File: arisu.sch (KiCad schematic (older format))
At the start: 28 parts, among them J1 USB_B_Micro, J10 PF6, J11 PF7, J2 MISO, J3 VCC, J4 SCK, J5 MOSI, J6 RES, J7 GND, J8 PF4, J9 PF5, U1 USBLC6-2SC6, U2 ATmega32U4-AU, Y1 Crystal_GND24

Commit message: Assign PCB footprints to schematic symbols
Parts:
- C1, C2, C3, C4, C5, C6, C7, C8, C9: footprint (none) -> Capacitors_SMD:C_0805_HandSoldering
- J1: footprint (none) -> Connectors_USB:USB_Micro-B_Molex-105017-0001
- J10, J11, J2, J3, J4, J5, J6, J7, J8, J9: footprint (none) -> Pin_Headers:Pin_Header_Straight_1x01_Pitch2.54mm
- R1, R2, R3, R4: footprint (none) -> Resistors_SMD:R_0805_HandSoldering
- SWR1: footprint (none) -> Buttons_Switches_SMD:SW_SPST_TL3342
- Y1: footprint (none) -> Crystals:Crystal_SMD_SeikoEpson_FA238-4pin_3.2x2.5mm_HandSoldering
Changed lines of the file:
@@
 F 0 "J1" H 1055 5267 50  0000 C CNN
 F 1 "USB_B_Micro" H 1055 5176 50  0000 C CNN
-F 2 "" H 1150 4750 50  0001 C CNN
+F 2 "Connectors_USB:USB_Micro-B_Molex-105017-0001" H 1150 4750 50  0001 C CNN
 F 3 "~" H 1150 4750 50  0001 C CNN
 	1    1000 4800
@@
 F 0 "R1" V 2550 4800 50  0000 C CNN
 F 1 "22" V 2650 4800 50  0000 C CNN
-F 2 "" V 2580 4800 50  0001 C CNN
+F 2 "Resistors_SMD:R_0805_HandSoldering" V 2580 4800 50  0001 C CNN
 F 3 "~" H 2650 4800 50  0001 C CNN
 	1    2650 4800
@@
 F 0 "R2" V 2750 4900 50  0000 C CNN
 F 1 "22" V 2650 4900 50  0000 C CNN
-F 2 "" V 2580 4900 50  0001 C CNN
+F 2 "Resistors_SMD:R_0805_HandSoldering" V 2580 4900 50  0001 C CNN
 F 3 "~" H 2650 4900 50  0001 C CNN
 	1    2650 4900
@@
 F 0 "C4" H 3765 4246 50  0000 L CNN
 F 1 "1uF (±10%)" H 3765 4155 50  0000 L CNN
-F 2 "" H 3688 4050 50  0001 C CNN
+F 2 "Capacitors_SMD:C_0805_HandSoldering" H 3688 4050 50  0001 C CNN
 F 3 "~" H 3650 4200 50  0001 C CNN
 	1    3650 4200
@@
 F 0 "Y1" H 1850 4000 50  0000 L CNN
 F 1 "Crystal_GND24" H 1650 3900 50  0000 L CNN
-F 2 "" H 1900 3650 50  0001 C CNN
+F 2 "Crystals:Crystal_SMD_SeikoEpson_FA238-4pin_3.2x2.5mm_HandSoldering" H 1900 3650 50  0001 C CNN
 F 3 "~" H 1900 3650 50  0001 C CNN
 	1    1900 3650
@@
 F 0 "C1" H 1436 3754 50  0000 R CNN
 F 1 "22pF" H 1436 3845 50  0000 R CNN
-F 2 "" H 1588 3650 50  0001 C CNN
+F 2 "Capacitors_SMD:C_0805_HandSoldering" H 1588 3650 50  0001 C CNN
 F 3 "~" H 1550 3800 50  0001 C CNN
 	1    1550 3800
@@
 F 0 "C2" H 2365 3846 50  0000 L CNN
 F 1 "22pF" H 2365 3755 50  0000 L CNN
-F 2 "" H 2288 3650 50  0001 C CNN
+F 2 "Capacitors_SMD:C_0805_HandSoldering" H 2288 3650 50  0001 C CNN
 F 3 "~" H 2250 3800 50  0001 C CNN
 	1    2250 3800
@@
 F 0 "C3" H 3365 4246 50  0000 L CNN
 F 1 "10uF" H 3365 4155 50  0000 L CNN
-F 2 "" H 3288 4050 50  0001 C CNN
+F 2 "Capacitors_SMD:C_0805_HandSoldering" H 3288 4050 50  0001 C CNN
 F 3 "~" H 3250 4200 50  0001 C CNN
 	1    3250 4200
@@
 F 0 "SWR1" H 3400 3035 50  0000 C CNN
 F 1 "SW_Push" H 3400 2944 50  0000 C CNN
-F 2 "" H 3400 2950 50  0001 C CNN
+F 2 "Buttons_Switches_SMD:SW_SPST_TL3342" H 3400 2950 50  0001 C CNN
 F 3 "" H 3400 2950 50  0001 C CNN
 	1    3400 2750
@@
 F 0 "R3" H 3870 2596 50  0000 L CNN
 F 1 "10K" V 3800 2500 50  0000 L CNN
-F 2 "" V 3730 2550 50  0001 C CNN
+F 2 "Resistors_SMD:R_0805_HandSoldering" V 3730 2550 50  0001 C CNN
 F 3 "~" H 3800 2550 50  0001 C CNN
 	1    3800 2550
@@
 F 0 "C5" H 5365 1196 50  0000 L CNN
 F 1 "1uF" H 5365 1105 50  0000 L CNN
-F 2 "" H 5288 1000 50  0001 C CNN
+F 2 "Capacitors_SMD:C_0805_HandSoldering" H 5288 1000 50  0001 C CNN
 F 3 "~" H 5250 1150 50  0001 C CNN
 	1    5250 1150
@@
 F 0 "C6" H 5365 1746 50  0000 L CNN
 F 1 "0.1uF" H 5365 1655 50  0000 L CNN
-F 2 "" H 5288 1550 50  0001 C CNN
+F 2 "Capacitors_SMD:C_0805_HandSoldering" H 5288 1550 50  0001 C CNN
 F 3 "~" H 5250 1700 50  0001 C CNN
 	1    5250 1700
@@
 F 0 "C8" H 5815 1746 50  0000 L CNN
 F 1 "0.1uF" H 5815 1655 50  0000 L CNN
-F 2 "" H 5738 1550 50  0001 C CNN
+F 2 "Capacitors_SMD:C_0805_HandSoldering" H 5738 1550 50  0001 C CNN
 F 3 "~" H 5700 1700 50  0001 C CNN
 	1    5700 1700
@@
 F 0 "C7" H 5365 2296 50  0000 L CNN
 F 1 "0.1uF" H 5365 2205 50  0000 L CNN
-F 2 "" H 5288 2100 50  0001 C CNN
+F 2 "Capacitors_SMD:C_0805_HandSoldering" H 5288 2100 50  0001 C CNN
 F 3 "~" H 5250 2250 50  0001 C CNN
 	1    5250 2250
@@
 F 0 "C9" H 5815 2296 50  0000 L CNN
 F 1 "0.1uF" H 5815 2205 50  0000 L CNN
-F 2 "" H 5738 2100 50  0001 C CNN
+F 2 "Capacitors_SMD:C_0805_HandSoldering" H 5738 2100 50  0001 C CNN
 F 3 "~" H 5700 2250 50  0001 C CNN
 	1    5700 2250
@@
 F 0 "R4" H 5770 5946 50  0000 L CNN
 F 1 "10K" V 5700 5850 50  0000 L CNN
-F 2 "" V 5630 5900 50  0001 C CNN
+F 2 "Resistors_SMD:R_0805_HandSoldering" V 5630 5900 50  0001 C CNN
 F 3 "~" H 5700 5900 50  0001 C CNN
 	1    5700 5900
@@
 F 0 "J8" H 6179 6642 50  0000 L CNN
 F 1 "PF4" H 6179 6551 50  0000 L CNN
-F 2 "" H 6100 6600 50  0001 C CNN
+F 2 "Pin_Headers:Pin_Header_Straight_1x01_Pitch2.54mm" H 6100 6600 50  0001 C CNN
 F 3 "~" H 6100 6600 50  0001 C CNN
 	1    6100 6600
@@
 F 0 "J9" H 6179 6842 50  0000 L CNN
 F 1 "PF5" H 6179 6751 50  0000 L CNN
-F 2 "" H 6100 6800 50  0001 C CNN
+F 2 "Pin_Headers:Pin_Header_Straight_1x01_Pitch2.54mm" H 6100 6800 50  0001 C CNN
 F 3 "~" H 6100 6800 50  0001 C CNN
 	1    6100 6800
@@
 F 0 "J10" H 6179 7042 50  0000 L CNN
 F 1 "PF6" H 6179 6951 50  0000 L CNN
-F 2 "" H 6100 7000 50  0001 C CNN
+F 2 "Pin_Headers:Pin_Header_Straight_1x01_Pitch2.54mm" H 6100 7000 50  0001 C CNN
 F 3 "~" H 6100 7000 50  0001 C CNN
 	1    6100 7000
@@
 F 0 "J11" H 6179 7242 50  0000 L CNN
 F 1 "PF7" H 6179 7151 50  0000 L CNN
-F 2 "" H 6100 7200 50  0001 C CNN
+F 2 "Pin_Headers:Pin_Header_Straight_1x01_Pitch2.54mm" H 6100 7200 50  0001 C CNN
 F 3 "~" H 6100 7200 50  0001 C CNN
 	1    6100 7200
@@
 F 0 "J2" H 3050 850 50  0000 C CNN
 F 1 "MISO" H 3050 950 50  0000 C CNN
-F 2 "" H 2900 900 50  0001 C CNN
+F 2 "Pin_Headers:Pin_Header_Straight_1x01_Pitch2.54mm" H 2900 900 50  0001 C CNN
 F 3 "~" H 2900 900 50  0001 C CNN
 	1    2900 900
@@
 F 0 "J3" H 3050 1050 50  0000 C CNN
 F 1 "VCC" H 3050 1150 50  0000 C CNN
-F 2 "" H 2900 1100 50  0001 C CNN
+F 2 "Pin_Headers:Pin_Header_Straight_1x01_Pitch2.54mm" H 2900 1100 50  0001 C CNN
 F 3 "~" H 2900 1100 50  0001 C CNN
 	1    2900 1100
@@
 F 0 "J4" H 3050 1250 50  0000 C CNN
 F 1 "SCK" H 3050 1350 50  0000 C CNN
-F 2 "" H 2900 1300 50  0001 C CNN
+F 2 "Pin_Headers:Pin_Header_Straight_1x01_Pitch2.54mm" H 2900 1300 50  0001 C CNN
 F 3 "~" H 2900 1300 50  0001 C CNN
 	1    2900 1300
@@
 F 0 "J5" H 3050 1450 50  0000 C CNN
 F 1 "MOSI" H 3050 1550 50  0000 C CNN
-F 2 "" H 2900 1500 50  0001 C CNN
+F 2 "Pin_Headers:Pin_Header_Straight_1x01_Pitch2.54mm" H 2900 1500 50  0001 C CNN
 F 3 "~" H 2900 1500 50  0001 C CNN
 	1    2900 1500
@@
 F 0 "J6" H 3050 1650 50  0000 C CNN
 F 1 "RES" H 3050 1750 50  0000 C CNN
-F 2 "" H 2900 1700 50  0001 C CNN
+F 2 "Pin_Headers:Pin_Header_Straight_1x01_Pitch2.54mm" H 2900 1700 50  0001 C CNN
 F 3 "~" H 2900 1700 50  0001 C CNN
 	1    2900 1700
@@
 F 0 "J7" H 3050 1850 50  0000 C CNN
 F 1 "GND" H 3050 1950 50  0000 C CNN
-F 2 "" H 2900 1900 50  0001 C CNN
+F 2 "Pin_Headers:Pin_Header_Straight_1x01_Pitch2.54mm" H 2900 1900 50  0001 C CNN
 F 3 "~" H 2900 1900 50  0001 C CNN
 	1    2900 1900

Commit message: Update ATMEGA32U4-AU and USBLC6-2SC6 footprints
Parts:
- U1: footprint Package_TO_SOT_SMD:SOT-23-6 -> TO_SOT_Packages_SMD:SOT-23-6_Handsoldering
- U2: footprint Package_QFP:TQFP-44_10x10mm_P0.8mm -> Housings_QFP:TQFP-44_10x10mm_Pitch0.8mm
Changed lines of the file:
@@
 F 0 "U2" H 4900 2400 50  0000 C CNN
 F 1 "ATmega32U4-AU" H 4900 2500 50  0000 C CNN
-F 2 "Package_QFP:TQFP-44_10x10mm_P0.8mm" H 4500 4250 50  0001 C CIN
+F 2 "Housings_QFP:TQFP-44_10x10mm_Pitch0.8mm" H 4500 4250 50  0001 C CIN
 F 3 "http://ww1.microchip.com/downloads/en/DeviceDoc/Atmel-7766-8-bit-AVR-ATmega16U4-32U4_Datasheet.pdf" H 4500 4250 50  0001 C CNN
 	1    4500 4250
@@
 F 0 "U1" H 1900 6328 50  0000 C CNN
 F 1 "USBLC6-2SC6" H 1900 6237 50  0000 C CNN
-F 2 "Package_TO_SOT_SMD:SOT-23-6" H 1150 6050 50  0001 C CNN
+F 2 "TO_SOT_Packages_SMD:SOT-23-6_Handsoldering" H 1150 6050 50  0001 C CNN
 F 3 "http://www2.st.com/resource/en/datasheet/CD00050750.pdf" H 2100 6000 50  0001 C CNN
 	1    1900 5650

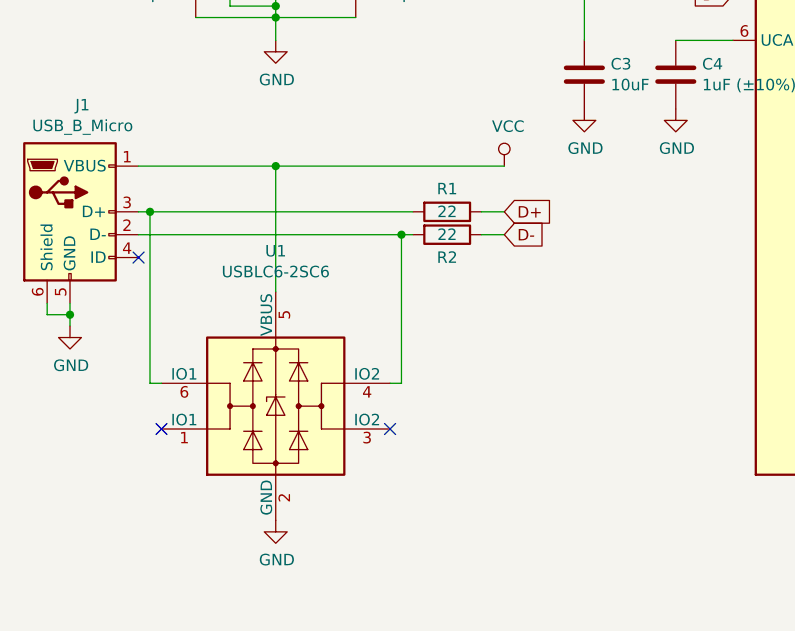
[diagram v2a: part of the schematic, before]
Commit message: Add D+/D- pin header to schematic
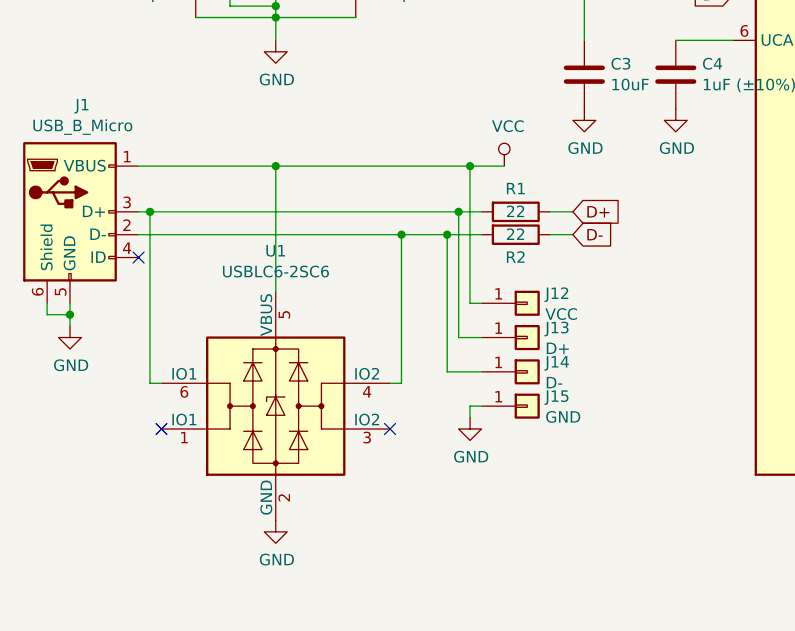
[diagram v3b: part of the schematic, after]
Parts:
- added J12: VCC, Pin_Headers:Pin_Header_Straight_1x01_Pitch2.54mm, symbol Connector_Generic:Conn_01x01
- added J13: D+, Pin_Headers:Pin_Header_Straight_1x01_Pitch2.54mm, symbol Connector_Generic:Conn_01x01
- added J14: D-, Pin_Headers:Pin_Header_Straight_1x01_Pitch2.54mm, symbol Connector_Generic:Conn_01x01
- added J15: GND, Pin_Headers:Pin_Header_Straight_1x01_Pitch2.54mm, symbol Connector_Generic:Conn_01x01
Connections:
- net GND: now also J15.1 (Pin_1)
- net VCC: now also J12.1 (Pin_1)
- net at J1.2 (D-), R2.2, U1.4 (IO2): now also J14.1 (Pin_1)
- net at J1.3 (D+), R1.2, U1.6 (IO1): now also J13.1 (Pin_1)
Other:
- moved on the sheet: R1, R2
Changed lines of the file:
@@
 L Device:R R1
 U 1 1 5C4B245D
-P 2650 4800
-F 0 "R1" V 2550 4800 50  0000 C CNN
-F 1 "22" V 2650 4800 50  0000 C CNN
-F 2 "Resistors_SMD:R_0805_HandSoldering" V 2580 4800 50  0001 C CNN
-F 3 "~" H 2650 4800 50  0001 C CNN
-	1    2650 4800
+P 2950 4800
+F 0 "R1" V 2850 4800 50  0000 C CNN
+F 1 "22" V 2950 4800 50  0000 C CNN
+F 2 "Resistors_SMD:R_0805_HandSoldering" V 2880 4800 50  0001 C CNN
+F 3 "~" H 2950 4800 50  0001 C CNN
+	1    2950 4800
 	0    1    1    0
 $EndComp
@@
 L Device:R R2
 U 1 1 5C4B25B0
-P 2650 4900
-F 0 "R2" V 2750 4900 50  0000 C CNN
-F 1 "22" V 2650 4900 50  0000 C CNN
-F 2 "Resistors_SMD:R_0805_HandSoldering" V 2580 4900 50  0001 C CNN
-F 3 "~" H 2650 4900 50  0001 C CNN
-	1    2650 4900
+P 2950 4900
+F 0 "R2" V 3050 4900 50  0000 C CNN
+F 1 "22" V 2950 4900 50  0000 C CNN
+F 2 "Resistors_SMD:R_0805_HandSoldering" V 2880 4900 50  0001 C CNN
+F 3 "~" H 2950 4900 50  0001 C CNN
+	1    2950 4900
 	0    1    1    0
 $EndComp
@@
 Connection ~ 1900 4600
 Wire Wire Line
-	2900 4600 1900 4600
-Text GLabel 2900 4800 2    50   Input ~ 0
+	2900 4600 2750 4600
+Text GLabel 3200 4800 2    50   Input ~ 0
 D+
 Wire Wire Line
-	2800 4800 2900 4800
-Text GLabel 2900 4900 2    50   Input ~ 0
+	3100 4800 3200 4800
+Text GLabel 3200 4900 2    50   Input ~ 0
 D-
 Wire Wire Line
-	2800 4900 2900 4900
+	3100 4900 3200 4900
 Wire Wire Line
 	1300 4800 1350 4800
@@
 Wire Wire Line
 	1350 5550 1350 4800
-Wire Wire Line
-	1350 4800 2500 4800
 Connection ~ 1350 4800
 Wire Wire Line
@@
 	2450 5550 2450 4900
 Connection ~ 2450 4900
-Wire Wire Line
-	2450 4900 2500 4900
 $Comp
 L power:GND #PWR0102
@@
 NoConn ~ 1400 5750
 NoConn ~ 2400 5750
+$Comp
+L Connector_Generic:Conn_01x01 J13
+U 1 1 5C4E1CA1
+P 3000 5350
+F 0 "J13" H 3079 5392 50  0000 L CNN
+F 1 "D+" H 3079 5301 50  0000 L CNN
+F 2 "Pin_Headers:Pin_Header_Straight_1x01_Pitch2.54mm" H 3000 5350 50  0001 C CNN
+F 3 "~" H 3000 5350 50  0001 C CNN
+	1    3000 5350
+	1    0    0    -1
+$EndComp
+Wire Wire Line
+	1350 4800 2700 4800
+Wire Wire Line
+	2450 4900 2650 4900
+$Comp
+L Connector_Generic:Conn_01x01 J14
+U 1 1 5C4F0ABE
+P 3000 5500
+F 0 "J14" H 3079 5542 50  0000 L CNN
+F 1 "D-" H 3079 5451 50  0000 L CNN
+F 2 "Pin_Headers:Pin_Header_Straight_1x01_Pitch2.54mm" H 3000 5500 50  0001 C CNN
+F 3 "~" H 3000 5500 50  0001 C CNN
+	1    3000 5500
+	1    0    0    -1
+$EndComp
+$Comp
+L Connector_Generic:Conn_01x01 J12
+U 1 1 5C505CBA
+P 3000 5200
+F 0 "J12" H 3079 5242 50  0000 L CNN
+F 1 "VCC" H 3079 5151 50  0000 L CNN
+F 2 "Pin_Headers:Pin_Header_Straight_1x01_Pitch2.54mm" H 3000 5200 50  0001 C CNN
+F 3 "~" H 3000 5200 50  0001 C CNN
+	1    3000 5200
+	1    0    0    -1
+$EndComp
+$Comp
+L Connector_Generic:Conn_01x01 J15
+U 1 1 5C505D0A
+P 3000 5650
+F 0 "J15" H 3079 5692 50  0000 L CNN
+F 1 "GND" H 3079 5601 50  0000 L CNN
+F 2 "Pin_Headers:Pin_Header_Straight_1x01_Pitch2.54mm" H 3000 5650 50  0001 C CNN
+F 3 "~" H 3000 5650 50  0001 C CNN
+	1    3000 5650
+	1    0    0    -1
+$EndComp
+Wire Wire Line
+	2800 5200 2750 5200
+Wire Wire Line
+	2750 5200 2750 4600
+Connection ~ 2750 4600
+Wire Wire Line
+	2750 4600 1900 4600
+Wire Wire Line
+	2800 5350 2700 5350
+Wire Wire Line
+	2700 5350 2700 4800
+Connection ~ 2700 4800
+Wire Wire Line
+	2700 4800 2800 4800
+Wire Wire Line
+	2800 5500 2650 5500
+Wire Wire Line
+	2650 5500 2650 4900
+Connection ~ 2650 4900
+Wire Wire Line
+	2650 4900 2800 4900
+Wire Wire Line
+	2800 5650 2750 5650
+Wire Wire Line
+	2750 5650 2750 5700
 Wire Bus Line
 	5750 2700 5750 3150
@@
 	5500 5350 5500 7400
 Wire Bus Line
+	6750 2750 6750 5800
+Wire Bus Line
 	7050 2650 7050 5800
-Wire Bus Line
-	6750 2750 6750 5800
+$Comp
+L power:GND #PWR01
+U 1 1 5C51C1AD
+P 2750 5700
+F 0 "#PWR01" H 2750 5450 50  0001 C CNN
+F 1 "GND" H 2755 5527 50  0000 C CNN
+F 2 "" H 2750 5700 50  0001 C CNN
+F 3 "" H 2750 5700 50  0001 C CNN
+	1    2750 5700
+	1    0    0    -1
+$EndComp
 $EndSCHEMATC

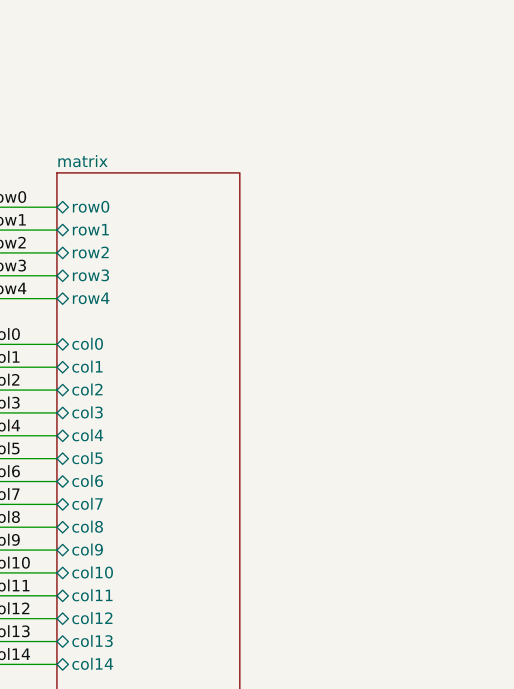
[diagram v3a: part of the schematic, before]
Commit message: Add mounting holes in schematic
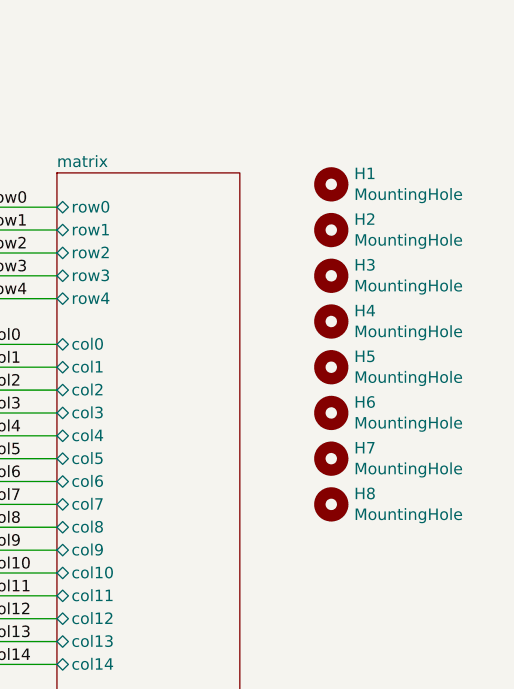
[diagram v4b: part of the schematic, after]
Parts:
- added H1, H2, H3, H4, H5, H6, H7, H8: MountingHole, Mounting_Holes:MountingHole_2.2mm_M2_Pad, symbol Mechanical:MountingHole
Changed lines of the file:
@@
 Wire Wire Line
 	2750 5650 2750 5700
+$Comp
+L power:GND #PWR01
+U 1 1 5C51C1AD
+P 2750 5700
+F 0 "#PWR01" H 2750 5450 50  0001 C CNN
+F 1 "GND" H 2755 5527 50  0000 C CNN
+F 2 "" H 2750 5700 50  0001 C CNN
+F 3 "" H 2750 5700 50  0001 C CNN
+	1    2750 5700
+	1    0    0    -1
+$EndComp
+$Comp
+L Mechanical:MountingHole H1
+U 1 1 5C583EFC
+P 8700 2700
+F 0 "H1" H 8800 2746 50  0000 L CNN
+F 1 "MountingHole" H 8800 2655 50  0000 L CNN
+F 2 "Mounting_Holes:MountingHole_2.2mm_M2_Pad" H 8700 2700 50  0001 C CNN
+F 3 "~" H 8700 2700 50  0001 C CNN
+	1    8700 2700
+	1    0    0    -1
+$EndComp
+$Comp
+L Mechanical:MountingHole H2
+U 1 1 5C584371
+P 8700 2900
+F 0 "H2" H 8800 2946 50  0000 L CNN
+F 1 "MountingHole" H 8800 2855 50  0000 L CNN
+F 2 "Mounting_Holes:MountingHole_2.2mm_M2_Pad" H 8700 2900 50  0001 C CNN
+F 3 "~" H 8700 2900 50  0001 C CNN
+	1    8700 2900
+	1    0    0    -1
+$EndComp
 Wire Bus Line
 	5750 2700 5750 3150
@@
 	7050 2650 7050 5800
 $Comp
-L power:GND #PWR01
-U 1 1 5C51C1AD
-P 2750 5700
-F 0 "#PWR01" H 2750 5450 50  0001 C CNN
-F 1 "GND" H 2755 5527 50  0000 C CNN
-F 2 "" H 2750 5700 50  0001 C CNN
-F 3 "" H 2750 5700 50  0001 C CNN
-	1    2750 5700
+L Mechanical:MountingHole H3
+U 1 1 5C59C18D
+P 8700 3100
+F 0 "H3" H 8800 3146 50  0000 L CNN
+F 1 "MountingHole" H 8800 3055 50  0000 L CNN
+F 2 "Mounting_Holes:MountingHole_2.2mm_M2_Pad" H 8700 3100 50  0001 C CNN
+F 3 "~" H 8700 3100 50  0001 C CNN
+	1    8700 3100
 	1    0    0    -1
 $EndComp
+$Comp
+L Mechanical:MountingHole H4
+U 1 1 5C59C1E9
+P 8700 3300
+F 0 "H4" H 8800 3346 50  0000 L CNN
+F 1 "MountingHole" H 8800 3255 50  0000 L CNN
+F 2 "Mounting_Holes:MountingHole_2.2mm_M2_Pad" H 8700 3300 50  0001 C CNN
+F 3 "~" H 8700 3300 50  0001 C CNN
+	1    8700 3300
+	1    0    0    -1
+$EndComp
+$Comp
+L Mechanical:MountingHole H5
+U 1 1 5C59C249
+P 8700 3500
+F 0 "H5" H 8800 3546 50  0000 L CNN
+F 1 "MountingHole" H 8800 3455 50  0000 L CNN
+F 2 "Mounting_Holes:MountingHole_2.2mm_M2_Pad" H 8700 3500 50  0001 C CNN
+F 3 "~" H 8700 3500 50  0001 C CNN
+	1    8700 3500
+	1    0    0    -1
+$EndComp
+$Comp
+L Mechanical:MountingHole H6
+U 1 1 5C59C2A7
+P 8700 3700
+F 0 "H6" H 8800 3746 50  0000 L CNN
+F 1 "MountingHole" H 8800 3655 50  0000 L CNN
+F 2 "Mounting_Holes:MountingHole_2.2mm_M2_Pad" H 8700 3700 50  0001 C CNN
+F 3 "~" H 8700 3700 50  0001 C CNN
+	1    8700 3700
+	1    0    0    -1
+$EndComp
+$Comp
+L Mechanical:MountingHole H7
+U 1 1 5C59C305
+P 8700 3900
+F 0 "H7" H 8800 3946 50  0000 L CNN
+F 1 "MountingHole" H 8800 3855 50  0000 L CNN
+F 2 "Mounting_Holes:MountingHole_2.2mm_M2_Pad" H 8700 3900 50  0001 C CNN
+F 3 "~" H 8700 3900 50  0001 C CNN
+	1    8700 3900
+	1    0    0    -1
+$EndComp
+$Comp
+L Mechanical:MountingHole H8
+U 1 1 5C59C367
+P 8700 4100
+F 0 "H8" H 8800 4146 50  0000 L CNN
+F 1 "MountingHole" H 8800 4055 50  0000 L CNN
+F 2 "Mounting_Holes:MountingHole_2.2mm_M2_Pad" H 8700 4100 50  0001 C CNN
+F 3 "~" H 8700 4100 50  0001 C CNN
+	1    8700 4100
+	1    0    0    -1
+$EndComp
